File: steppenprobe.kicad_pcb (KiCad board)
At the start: 2 copper layers, 50 x 60 mm, 88 parts, among them J1 USB_C_Receptacle_USB2.0, J2 Conn_ST_STDC14, J4 Conn_01x16, Q1 2N7002, SW1 SW_SPDT, SW2 SW_Push, U1 FT2232HL, U10 74LVC1G125, U11 74LVC1G125, U12 74LVC1G125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

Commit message: Tweak soldermask parameters
Clearence: 50um
Minimum width: 100um
And re-fill zones.
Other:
- rule pad_to_mask_clearance: 0.051 -> 0.05
- rule solder_mask_min_width: 0.25 -> 0.1
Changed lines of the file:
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@@
     (pad_size 1.524 1.524)
     (pad_drill 0.762)
-    (pad_to_mask_clearance 0.051)
-    (solder_mask_min_width 0.25)
+    (pad_to_mask_clearance 0.05)
+    (solder_mask_min_width 0.1)
     (aux_axis_origin 0 0)
     (visible_elements FFFFE77F)

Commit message: Update project to KiCad 6.0.0 format
It was using the interim 5.99 nightlies
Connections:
- J1 pad A8: Net-(J1-PadA8) -> unconnected-(J1-PadA8)
- J1 pad B8: Net-(J1-PadB8) -> unconnected-(J1-PadB8)
- J2 pad 1: Net-(J2-Pad1) -> unconnected-(J2-Pad1)
- J2 pad 2: Net-(J2-Pad2) -> unconnected-(J2-Pad2)
- J2 pad 9: Net-(J2-Pad9) -> unconnected-(J2-Pad9)
- U1 pad 26: Net-(U1-Pad26) -> unconnected-(U1-Pad26)
- U1 pad 29: Net-(U1-Pad29) -> unconnected-(U1-Pad29)
- U1 pad 30: Net-(U1-Pad30) -> unconnected-(U1-Pad30)
- U1 pad 34: Net-(U1-Pad34) -> unconnected-(U1-Pad34)
- U1 pad 36: Net-(U1-Pad36) -> unconnected-(U1-Pad36)
- U1 pad 43: Net-(U1-Pad43) -> unconnected-(U1-Pad43)
- U1 pad 44: Net-(U1-Pad44) -> unconnected-(U1-Pad44)
- U1 pad 45: Net-(U1-Pad45) -> unconnected-(U1-Pad45)
- U1 pad 46: Net-(U1-Pad46) -> unconnected-(U1-Pad46)
- U1 pad 48: Net-(U1-Pad48) -> unconnected-(U1-Pad48)
- U1 pad 52: Net-(U1-Pad52) -> unconnected-(U1-Pad52)
- U1 pad 53: Net-(U1-Pad53) -> unconnected-(U1-Pad53)
- U1 pad 57: Net-(U1-Pad57) -> unconnected-(U1-Pad57)
- U1 pad 58: Net-(U1-Pad58) -> unconnected-(U1-Pad58)
- U1 pad 59: Net-(U1-Pad59) -> unconnected-(U1-Pad59)
- U4 pad 6: Net-(U4-Pad6) -> unconnected-(U4-Pad6)
- U4 pad 7: Net-(U4-Pad7) -> unconnected-(U4-Pad7)
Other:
- net class Default removed
- net class Power removed
- board text added: "~{SRST}"
- board text removed: "~SRST"

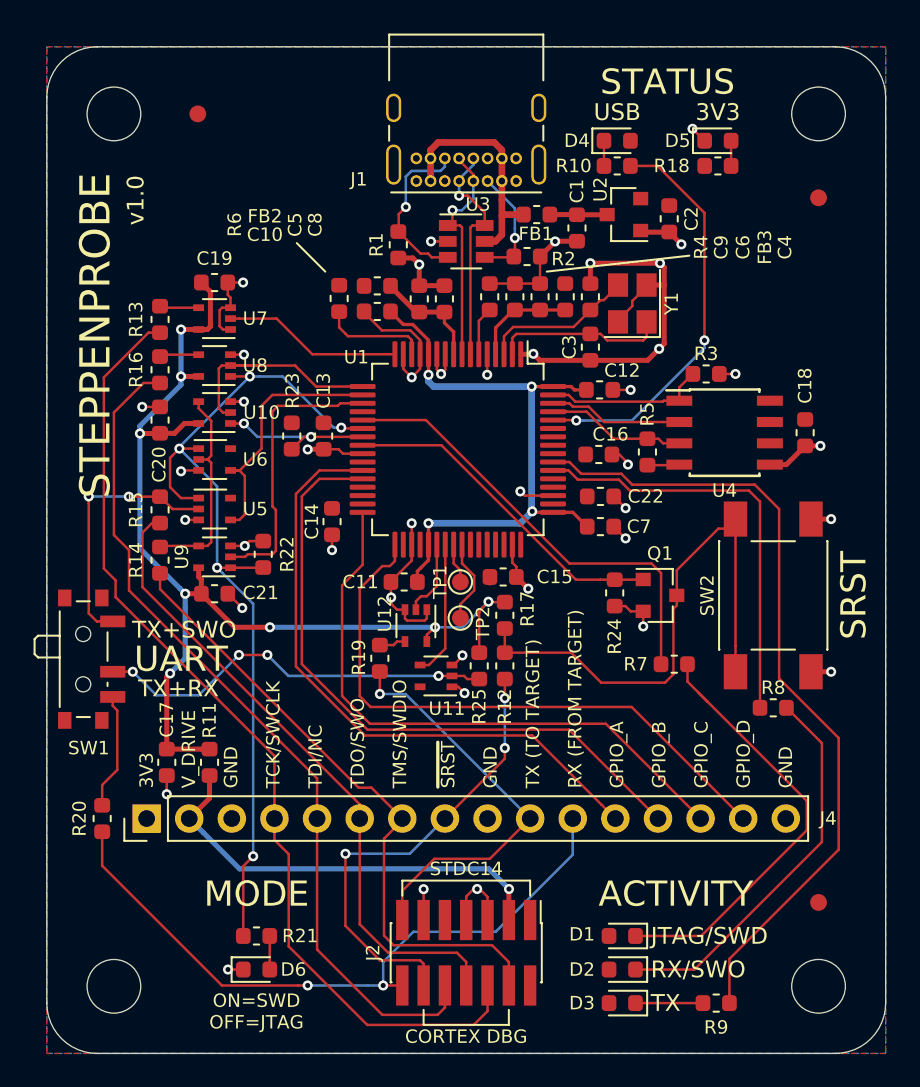
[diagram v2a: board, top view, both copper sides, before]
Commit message: Some cleanup after converting to KiCad 6.0
- Dangling tracks within pads
- SRST track had a clearance violation next to FTDI's pin 48,
by only a few microns. Touched slightly to fix it.
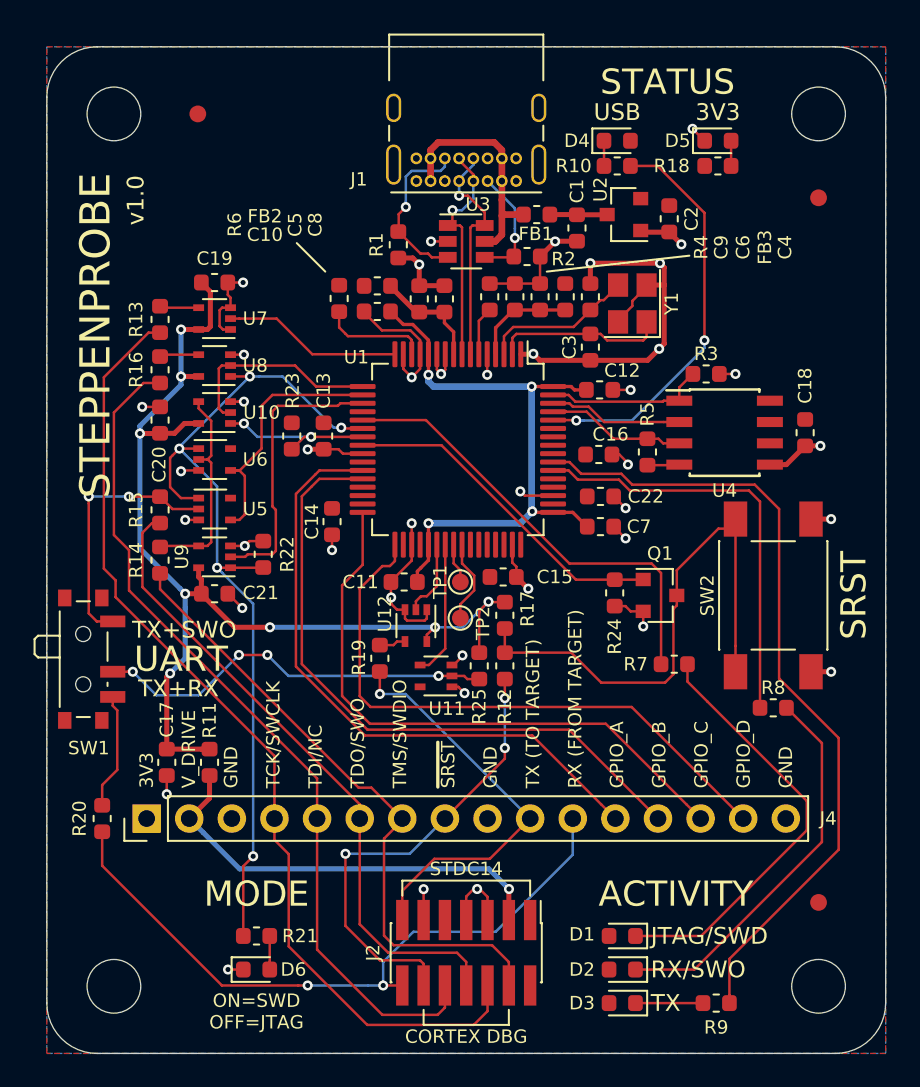
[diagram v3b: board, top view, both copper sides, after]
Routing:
- net /TDI: track 14.2 -> 12.3 mm
- net GND: track 107.2 -> 106.2 mm
- net /ACT_LED_K: track 26.4 -> 25.7 mm
